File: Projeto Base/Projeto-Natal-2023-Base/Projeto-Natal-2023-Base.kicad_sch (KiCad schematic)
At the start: 65 parts, among them J1 Conn_01x01_Pin, J2 Conn_01x01_Pin, J3 Conn_01x01_Pin, J4 Conn_01x01_Pin, J5 Conn_01x01_Pin, J6 Conn_01x01_Pin, J7 Conn_01x01_Pin, J8 Conn_01x01_Pin, Q1 BC817, Q2 BC817, Q3 BC817, Q4 BC817, Q5 MMBT3906, SW1 SW_Push, U1 CH32V003F4P6

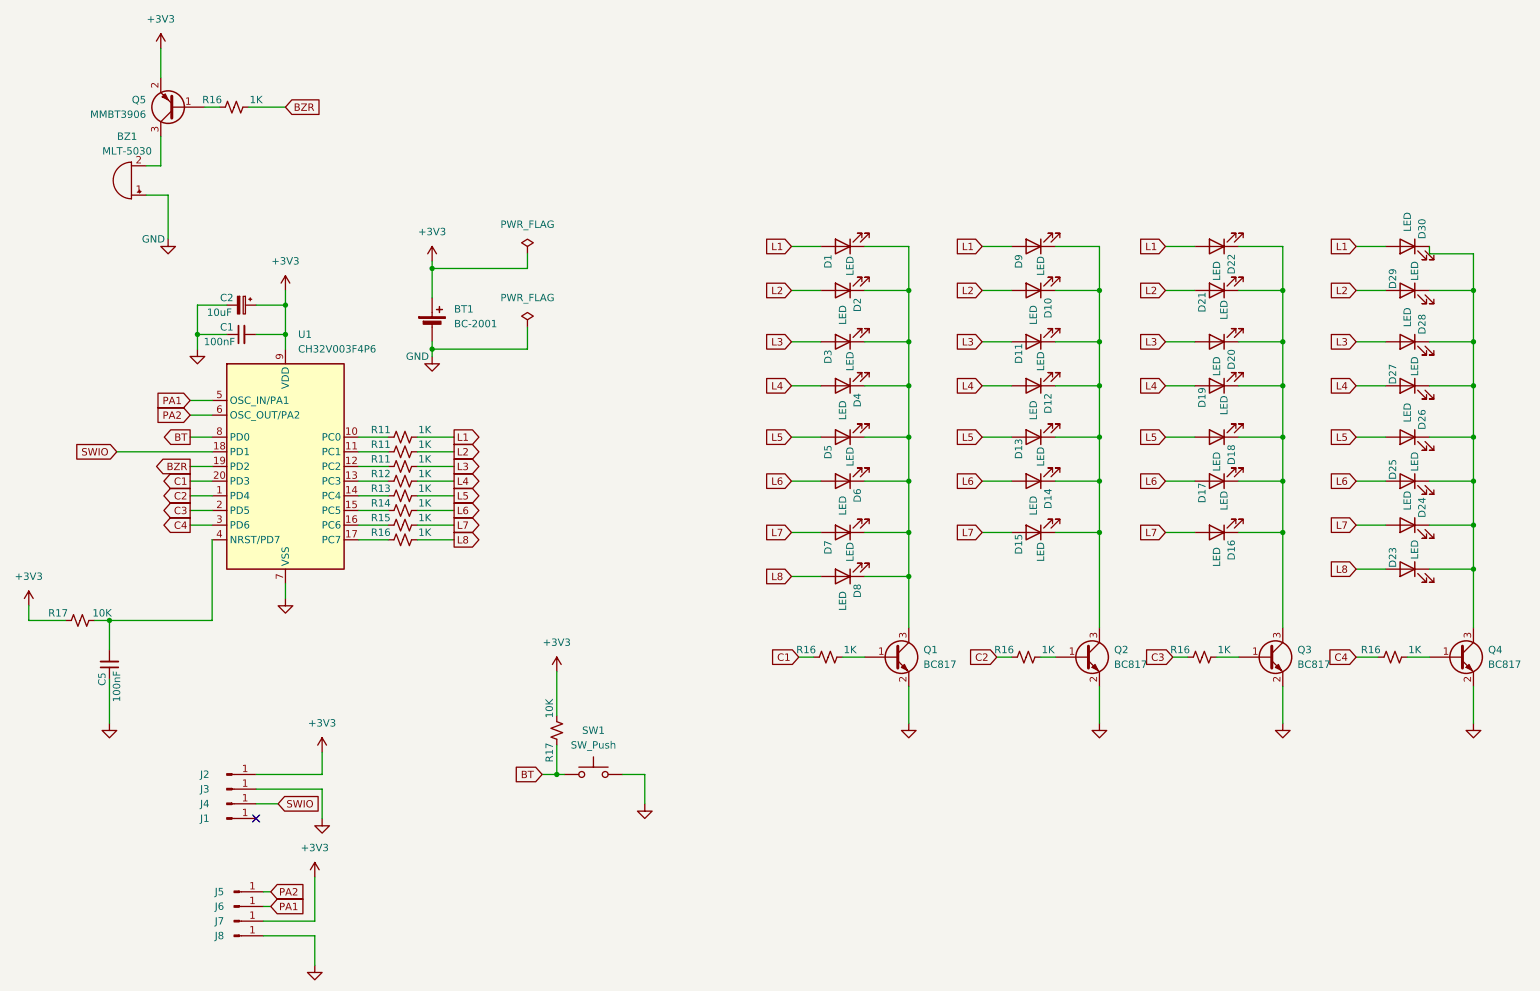
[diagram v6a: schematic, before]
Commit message: V1.1.0
Placa com 78,8 mm de diametro
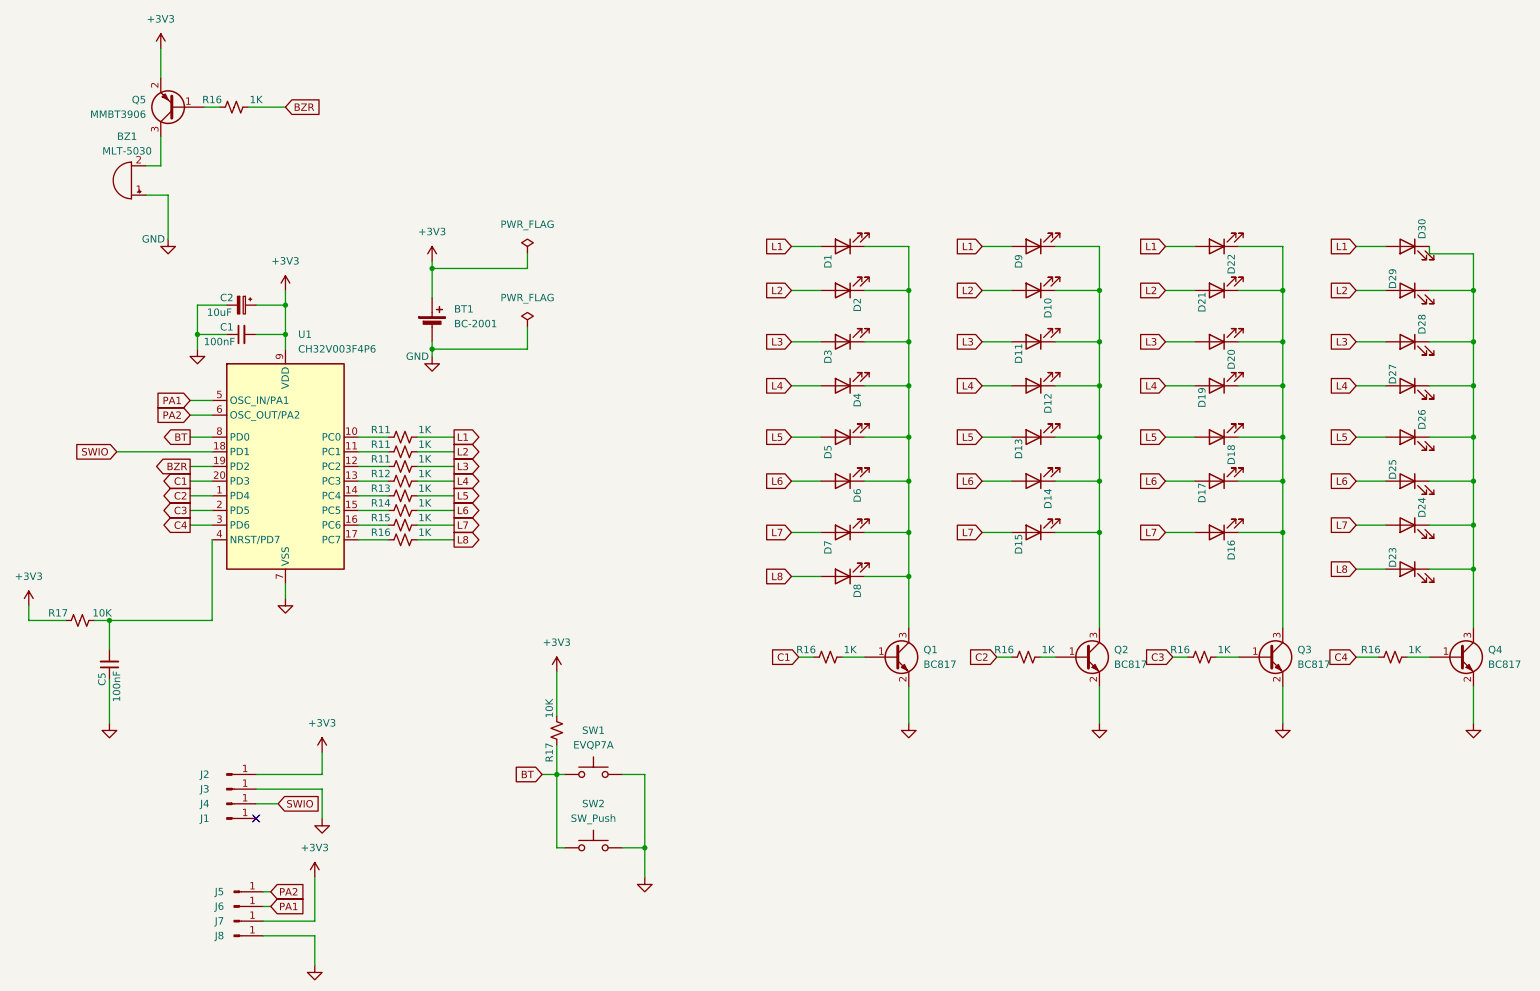
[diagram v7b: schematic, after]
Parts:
- added SW2: SW_Push, Button_Switch_SMD:SW_Push_1P1T_NO_6x6mm_H9.5mm, symbol Switch:SW_Push
- BT1: footprint Battery:BatteryHolder_Multicomp_BC-2001_1x2032 -> Battery:BatteryHolder_Keystone_3002_1x2032
- D1, D10, D13, D18, D21, D24, D27, D30, D4, D7: value LED -> D-B080508B1-KS2; LCSC (none) -> C108412
- D11, D14, D17, D2, D20, D23, D26, D29, D5, D8: value LED -> e17-21SURC/S530-A3/TR8; LCSC (none) -> C72037
- D12, D15, D16, D19, D22, D25, D28, D3, D6, D9: value LED -> NCD0805G1; LCSC (none) -> C84260
- SW1: value SW_Push -> EVQP7A; footprint Button_Switch_SMD:SW_Push_1P1T_NO_6x6mm_H9.5mm -> Button_Switch_SMD:SW_SPST_EVQP7A
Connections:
- net BT: now also SW2.1
- net GND: now also SW2.2
